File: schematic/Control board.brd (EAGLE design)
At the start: 37.1 x 55.9 mm, 14 parts, among them IC2 ATTINY44A

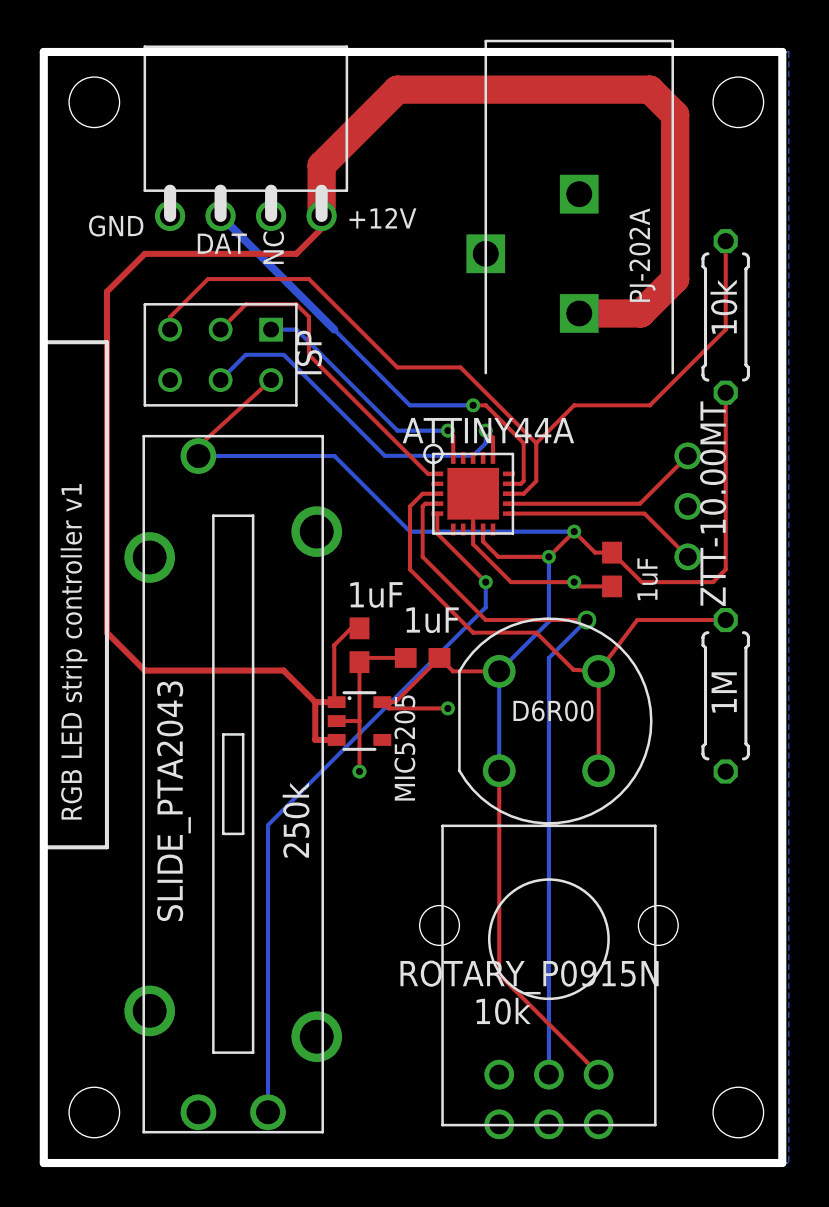
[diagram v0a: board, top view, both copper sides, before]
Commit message: Made the board a bit smaller, but there's still room to shrink it more
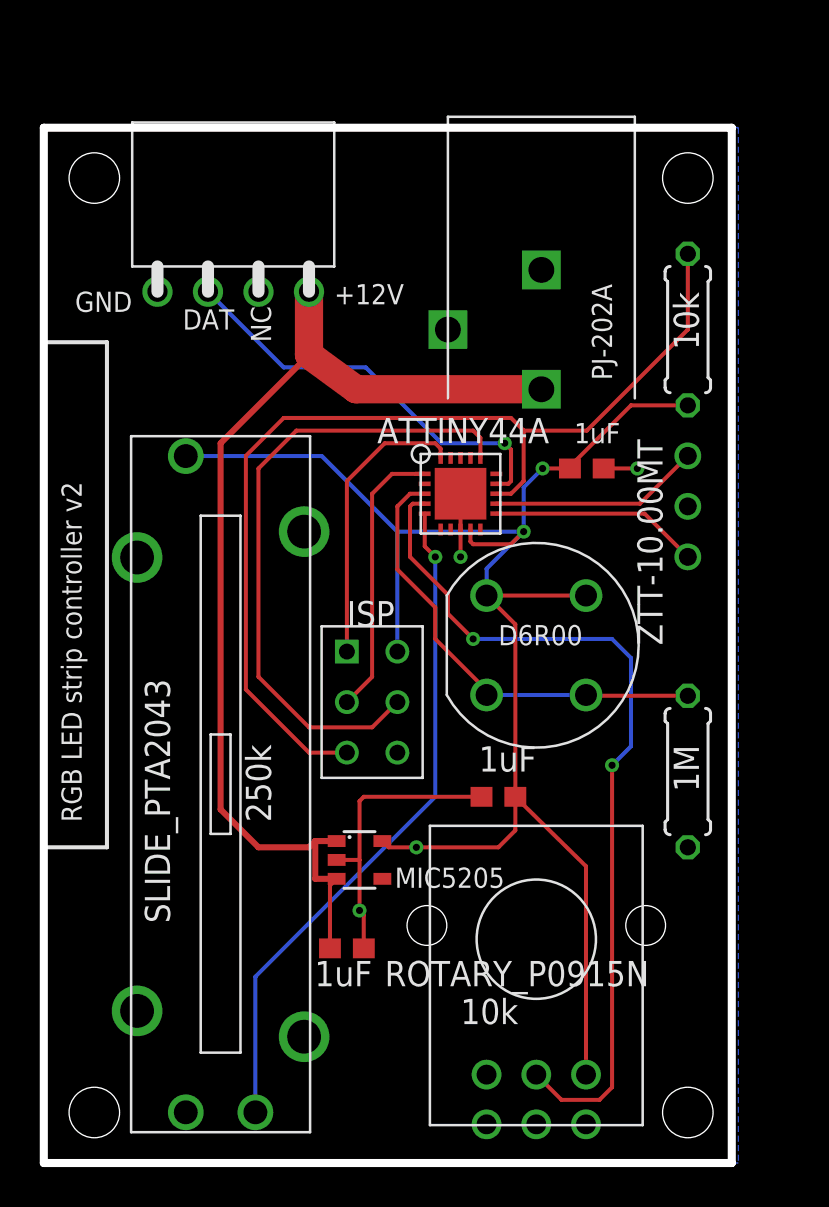
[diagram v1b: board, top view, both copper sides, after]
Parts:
- moved U$1 19.1 mm to (16.5, 23.2), turned to 0 degrees
- moved C1 15.3 mm to (15.2, 10.8), turned to 0 degrees
- moved C2 7.96 mm to (22.9, 18.4)
- moved REG1 6.99 mm to (15.9, 15.2)
- moved C3 5.24 mm to (27.3, 34.9), turned to 0 degrees
- moved POW1 4.26 mm to (20.3, 41.9)
- moved R1 4.26 mm to (32.4, 19.7)
- moved CONN1 3.86 mm to (9.53, 43.8)
- moved S1 3.86 mm to (24.8, 26.0)
- moved R3 2.01 mm to (32.4, 41.9)
- moved IC2 0.64 mm to (21.0, 33.7)
- moved SLIDE_PTA2043 0.63 mm to (8.89, 19.1)
- moved ROTARY_P0915N 0.63 mm to (24.8, 4.45)
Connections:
- net +5V: now also S1.1B; no longer S1.2A
- net COLOR_SW: now also S1.2A; no longer S1.1B
- net GND: no longer POW1.3
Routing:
- net +12V: track 86.6 -> 53.7 mm
- net MOSI: track 18.4 -> 32.2 mm, vias 1 -> 0
- net RESET: track 43.1 -> 51.5 mm
- net ROT_V: track 36.6 -> 43.7 mm, vias 1 -> 2
- net COLOR_SW: track 29.1 -> 23.1 mm
- net +5V: track 89.4 -> 84.4 mm
- net MISO: track 12.5 -> 14.7 mm, vias 1 -> 0
- net LED_SIGNAL: track 22.7 -> 20.9 mm
- net SLIDE_V: track 35.6 -> 34.1 mm
- net SCK: track 16.1 -> 14.5 mm
- net N$4: track 9.99 -> 10.6 mm
- net N$2: track 9.90 -> 10.5 mm
- net GND: vias 2 -> 3
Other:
- board size 37.1 x 55.9 mm -> 34.6 x 52.1 mm
- board text added: "RGB LED strip controller v2"
- board text removed: "RGB LED strip controller v1"

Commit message: Reduced the size of the control board
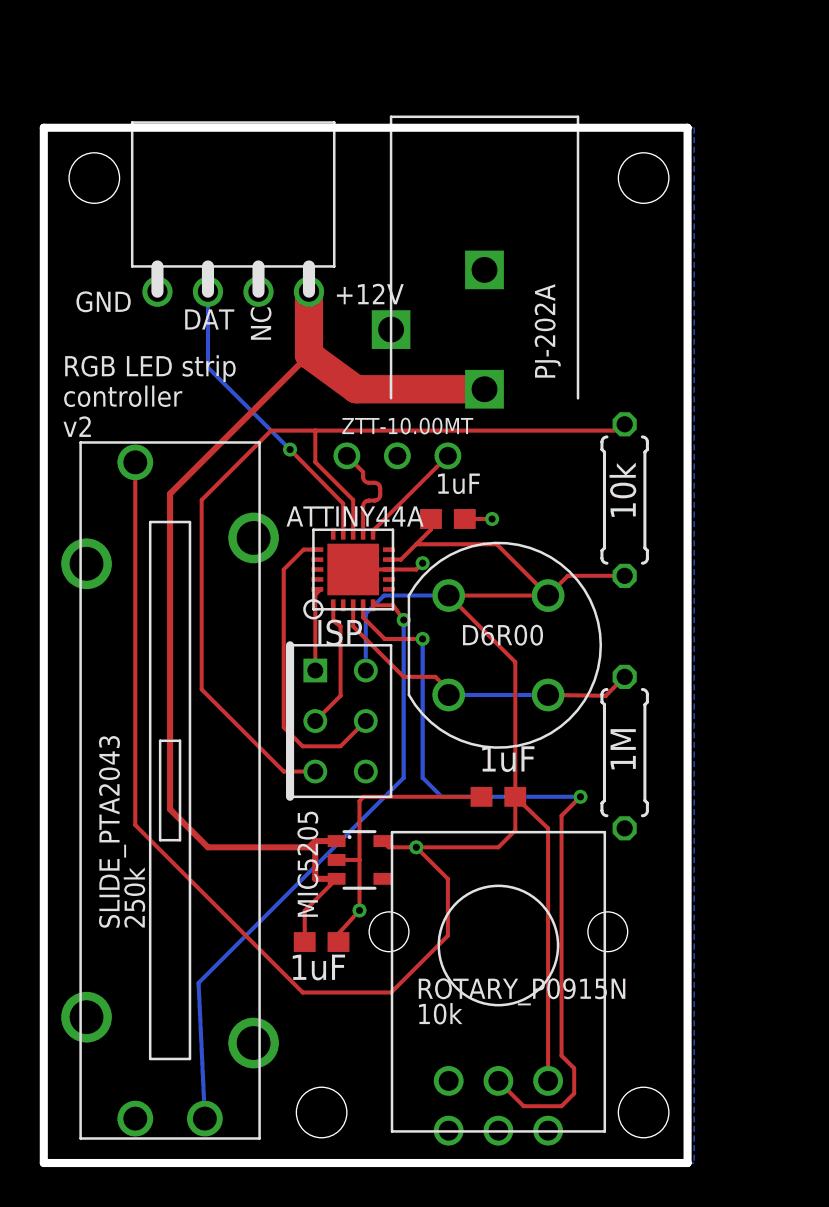
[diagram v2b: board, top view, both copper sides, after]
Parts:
- moved RES1 14.8 mm to (17.8, 35.6), turned to 180 degrees
- moved R3 9.14 mm to (29.2, 33.3)
- moved C3 7.43 mm to (20.3, 32.4)
- moved IC2 6.61 mm to (15.6, 29.8), turned to 90 degrees
- moved R1 3.31 mm to (29.2, 20.6)
- moved POW1 2.86 mm to (17.5, 41.9)
- moved SLIDE_PTA2043 2.56 mm to (6.35, 18.7)
- moved ROTARY_P0915N 1.93 mm to (22.9, 4.13)
- moved S1 1.91 mm to (22.9, 26.0)
- moved U$1 1.85 mm to (14.9, 22.2)
- moved C1 1.31 mm to (14.0, 11.1)
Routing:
- net +5V: track 84.4 -> 106.7 mm, vias 3 -> 1
- net MOSI: track 32.2 -> 15.1 mm
- net MISO: track 14.7 -> 4.36 mm
- net SCK: track 14.5 -> 6.53 mm
- net COLOR_SW: track 23.1 -> 16.7 mm
- net LED_SIGNAL: track 20.9 -> 15.0 mm
- net RESET: track 51.5 -> 45.8 mm
- net N$4: track 10.6 -> 5.29 mm
- net N$2: track 10.5 -> 5.47 mm
- net ROT_V: track 43.7 -> 39.5 mm
- net SLIDE_V: track 34.1 -> 31.3 mm
- net +12V: track 53.7 -> 54.6 mm
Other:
- board size 34.6 x 52.1 mm -> 32.4 x 52.1 mm

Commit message: Straightened a wire
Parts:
- moved POW1 0.95 mm to (18.4, 41.9)
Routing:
- net +5V: track 106.7 -> 105.4 mm
- net +12V: track 54.6 -> 55.6 mm
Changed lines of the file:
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@@
 <element name="CONN1" library="RGB LED project" package="S5440" value="4-PIN-RIGHT-ANGLE" x="9.525" y="43.815" smashed="yes"/>
 <element name="IC2" library="RGB LED project" package="QFN-20" value="ATTINY44A" x="15.5575" y="29.845" smashed="yes" rot="R90">
-<attribute name="VALUE" x="19.1135" y="33.02" size="1.016" layer="21" font="vector" ratio="10" rot="R180"/>
+<attribute name="VALUE" x="19.1135" y="33.655" size="1.016" layer="21" font="vector" ratio="10" rot="R180"/>
 </element>
-<element name="POW1" library="RGB LED project" package="PJ202A" value="PJ-202A" x="17.4625" y="41.91" smashed="yes" rot="R90">
-<attribute name="VALUE" x="25.7175" y="39.37" size="1.016" layer="21" font="vector" rot="R90"/>
+<element name="POW1" library="RGB LED project" package="PJ202A" value="PJ-202A" x="18.415" y="41.91" smashed="yes" rot="R90">
+<attribute name="VALUE" x="26.67" y="39.37" size="1.016" layer="21" font="vector" rot="R90"/>
 </element>
 <element name="R1" library="resistor" package="0207/7" value="1M" x="29.21" y="20.6375" smashed="yes" rot="R90">
@@
 <wire x1="16.1925" y1="27.6225" x2="16.1925" y2="24.765" width="0.2032" layer="16"/>
 <wire x1="4.6" y1="35.2325" x2="4.6" y2="16.99" width="0.2032" layer="1"/>
-<wire x1="4.6" y1="16.99" x2="13.0175" y2="8.5725" width="0.2032" layer="1"/>
-<wire x1="13.0175" y1="8.5725" x2="17.4625" y2="8.5725" width="0.2032" layer="1"/>
-<wire x1="17.4625" y1="8.5725" x2="20.32" y2="11.43" width="0.2032" layer="1"/>
-<wire x1="20.32" y1="11.43" x2="20.32" y2="14.2875" width="0.2032" layer="1"/>
-<wire x1="20.32" y1="14.2875" x2="18.7325" y2="15.875" width="0.2032" layer="1"/>
+<wire x1="4.6" y1="16.99" x2="12.3825" y2="9.2075" width="0.2032" layer="1"/>
+<wire x1="12.3825" y1="9.2075" x2="18.0975" y2="9.2075" width="0.2032" layer="1"/>
+<wire x1="18.0975" y1="9.2075" x2="19.3675" y2="10.4775" width="0.2032" layer="1"/>
+<wire x1="19.3675" y1="10.4775" x2="19.3675" y2="15.24" width="0.2032" layer="1"/>
+<wire x1="19.3675" y1="15.24" x2="18.7325" y2="15.875" width="0.2032" layer="1"/>
 </signal>
 <signal name="SLIDE_V">
 <contactref element="SLIDE_PTA2043" pad="P2"/>
 <contactref element="IC2" pad="P$5"/>
-<wire x1="8.1" y1="2.2325" x2="7.7825" y2="9.0525" width="0.2032" layer="16"/>
+<wire x1="8.1" y1="2.2325" x2="8.1" y2="9.37" width="0.2032" layer="16"/>
 <wire x1="18.0975" y1="19.3675" x2="18.0975" y2="27.305" width="0.2032" layer="16"/>
 <via x="18.0975" y="27.305" extent="1-16" drill="0.3556"/>
-<wire x1="18.0975" y1="19.3675" x2="7.7825" y2="9.0525" width="0.2032" layer="16"/>
+<wire x1="18.0975" y1="19.3675" x2="8.1" y2="9.37" width="0.2032" layer="16"/>
 <wire x1="16.5575" y1="28.045" x2="17.5675" y2="28.045" width="0.2032" layer="1"/>
 <wire x1="17.5675" y1="28.045" x2="18.0975" y2="27.305" width="0.2032" layer="1"/>
@@
 <wire x1="15.7" y1="38.91" x2="13.335" y2="40.64" width="1.4224" layer="1"/>
 <contactref element="POW1" pad="1"/>
-<wire x1="15.7" y1="38.91" x2="22.1625" y2="38.91" width="1.4224" layer="1"/>
+<wire x1="15.7" y1="38.91" x2="23.115" y2="38.91" width="1.4224" layer="1"/>
 <wire x1="13.12" y1="11.1125" x2="13.12" y2="12.685" width="0.2032" layer="1"/>
 <wire x1="13.12" y1="12.685" x2="14.725" y2="14.29" width="0.2032" layer="1"/>
